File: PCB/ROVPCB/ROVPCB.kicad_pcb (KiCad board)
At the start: 2 copper layers, 65 x 56 mm, 24 parts, among them J1 Conn_01x04_Male, J2 Conn_01x04_Male, J3 Conn_01x02_Male, J4 Conn_01x01_Male, P1 Conn_02x20_Odd_Even, U1 MPU-9250, U2 BME280, U3 LIGHT_TSL2591, U4 LTC4316IDDPBF, U5 AtlasOEM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

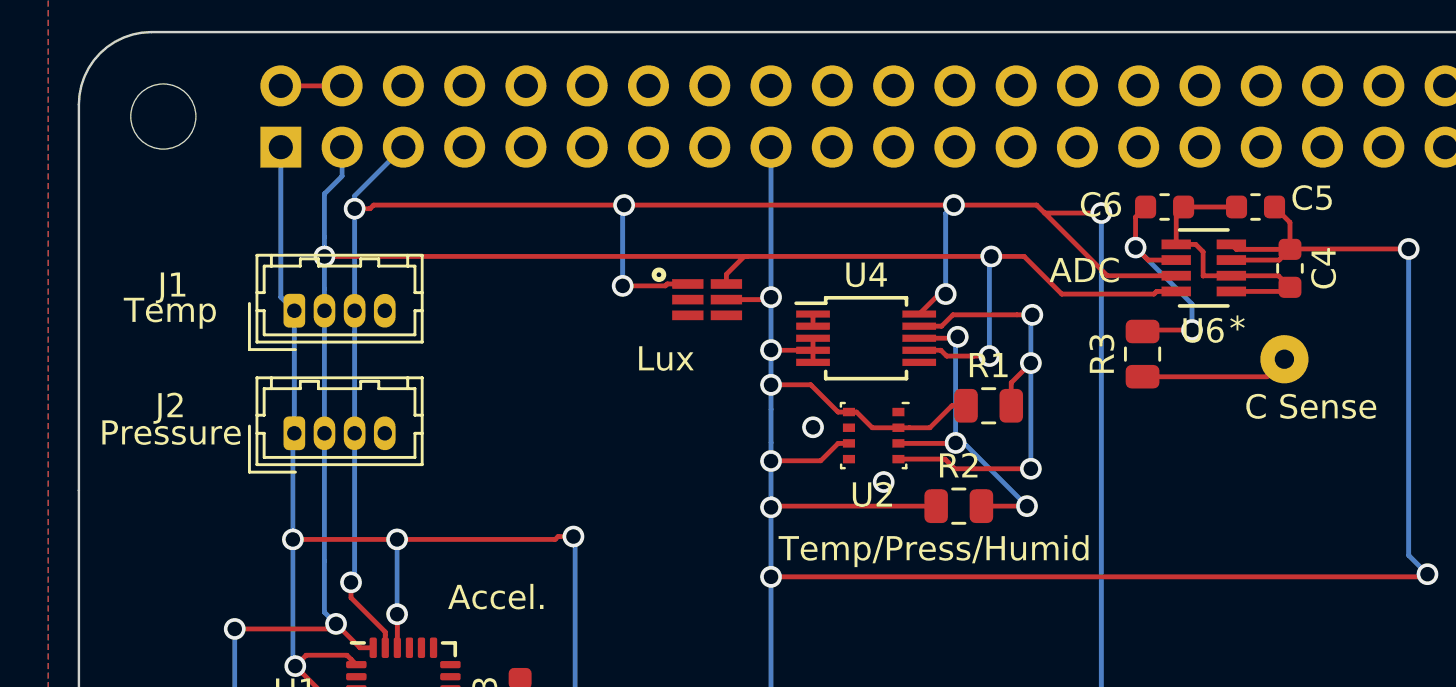
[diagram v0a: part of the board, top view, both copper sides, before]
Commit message: Stupid i2c inputs were flipped.....
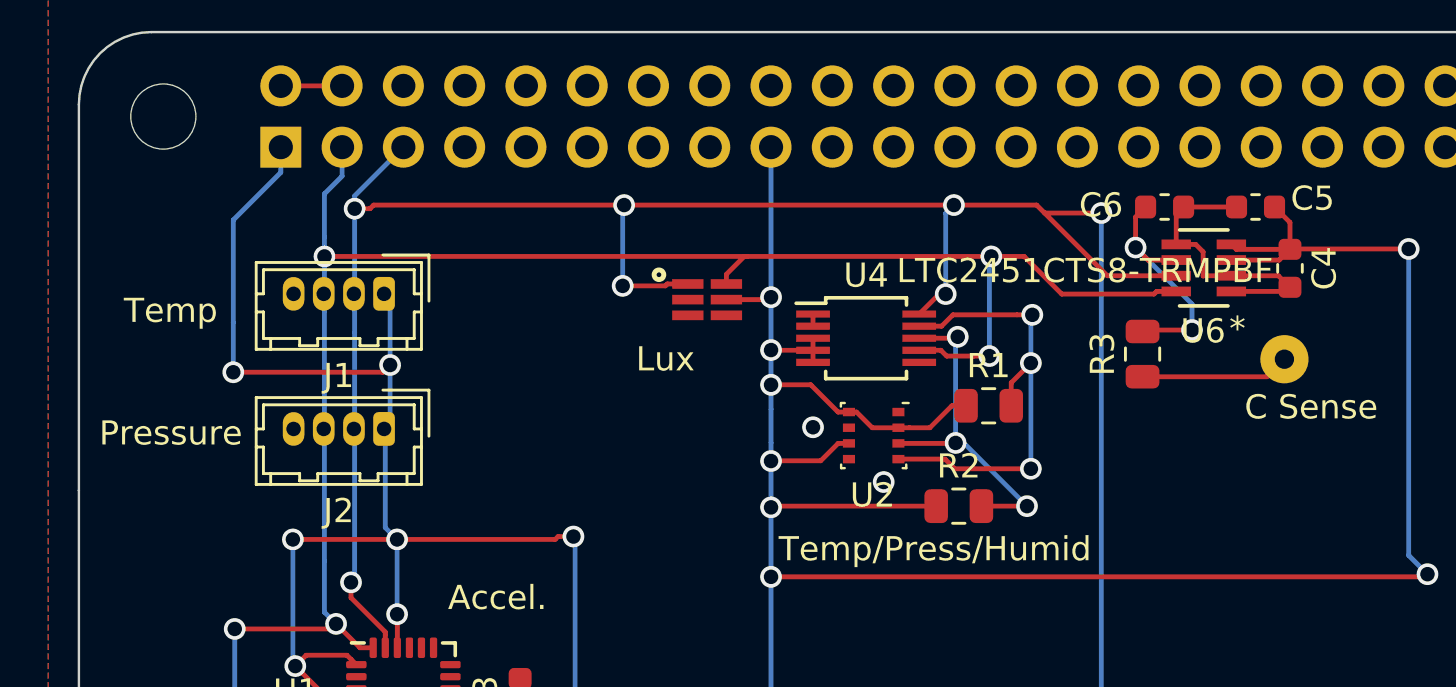
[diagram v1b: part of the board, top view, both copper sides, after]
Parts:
- U6: value ADC -> LTC2451CTS8-TRMPBF
- moved J1 3.79 mm to (212.7, 104.8), turned to 180 degrees
- moved J2 3.72 mm to (212.7, 110.5), turned to 180 degrees
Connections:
- J1 pad 2: /GPIO2(SDA1) -> /GPIO3(SCL1)
- J1 pad 3: /GPIO3(SCL1) -> /GPIO2(SDA1)
- J2 pad 2: /GPIO2(SDA1) -> /GPIO3(SCL1)
- J2 pad 3: /GPIO3(SCL1) -> /GPIO2(SDA1)
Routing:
- net +3V3: track 191.2 -> 202.1 mm, vias 16 -> 18

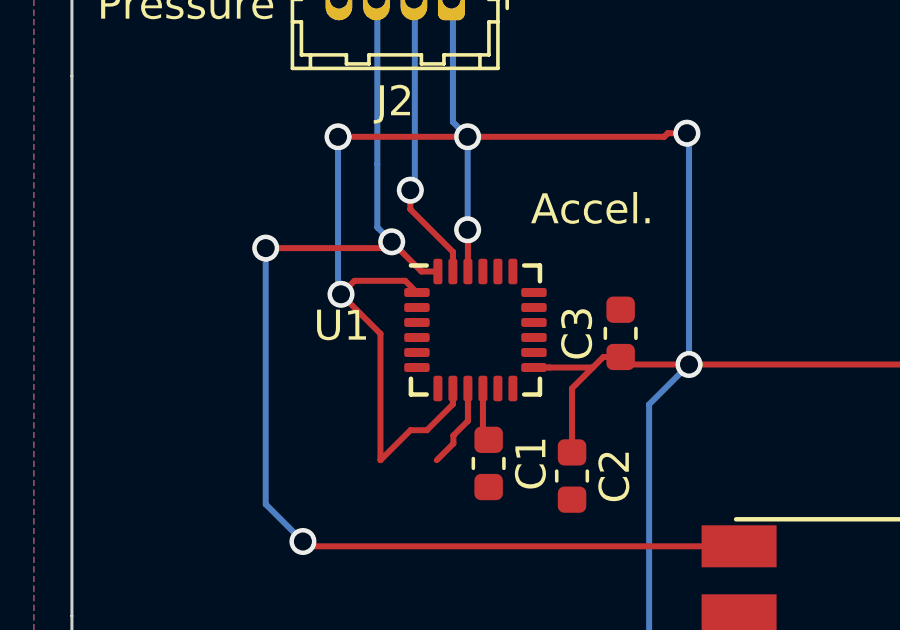
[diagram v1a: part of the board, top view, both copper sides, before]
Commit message: The correct footprint.... DUMB
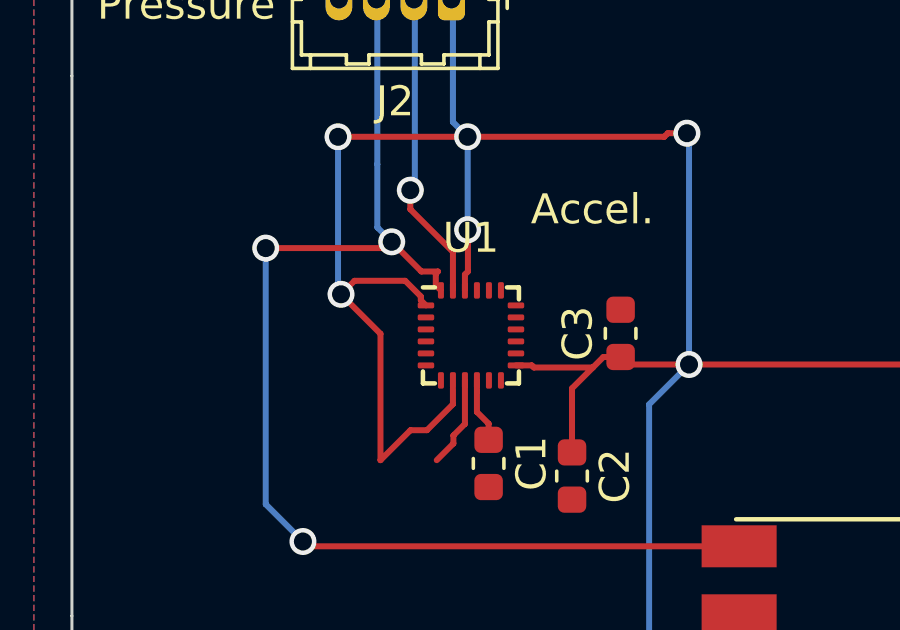
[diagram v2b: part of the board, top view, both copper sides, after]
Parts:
- U1: footprint Sensor_Motion:InvenSense_QFN-24_4x4mm_P0.5mm -> Sensor_Motion:InvenSense_QFN-24_3x3mm_P0.4mm
- moved U1 0.23 mm to (213.3, 121.7)
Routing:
- net +3V3: track 202.1 -> 203.9 mm
- net /GPIO2(SDA1): track 96.1 -> 96.9 mm
- net /GPIO3(SCL1): track 111.4 -> 112.0 mm
- net Net-(C1-Pad1): track 1.79 -> 2.41 mm
